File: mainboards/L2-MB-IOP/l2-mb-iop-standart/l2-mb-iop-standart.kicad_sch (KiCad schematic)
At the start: 46 parts, among them J1 URP_Conn_01x12_Socket, J10 GPP_Conn_01x12_Socket, J11 GPP_Conn_01x12_Socket, J12 GPP_Conn_01x12_Socket, J13 GPP_Conn_01x12_Socket, J14 GPP_Conn_01x12_Socket, J15 AIP_Conn_01x12_Socket, J16 AIP_Conn_01x12_Socket, J17 AIP_Conn_01x12_Socket, J18 AIP_Conn_01x12_Socket, J19 ICP_Conn_01x12_Socket, J2 URP_Conn_01x12_Socket, J20 ICP_Conn_01x12_Socket, J21 AIP_Conn_01x12_Socket, J22 AIP_Conn_01x12_Socket, J23 Conn_01x03_Pin, J24 Conn_01x02_Pin, J25 Conn_01x02_Pin, J26 Conn_01x02_Pin, J27 Conn_01x03_Pin, J28 Conn_01x02_Pin, J29 Conn_01x02_Pin, J3 GPP_Conn_01x12_Socket, J4 GPP_Conn_01x12_Socket, J5 GPP_Conn_01x12_Socket, J6 GPP_Conn_01x12_Socket, J7 GPP_Conn_01x12_Socket, J8 GPP_Conn_01x12_Socket, J9 GPP_Conn_01x12_Socket, SW1 SW_SPDT, U1 LM2596s_module, U2 LM2596_mini_module

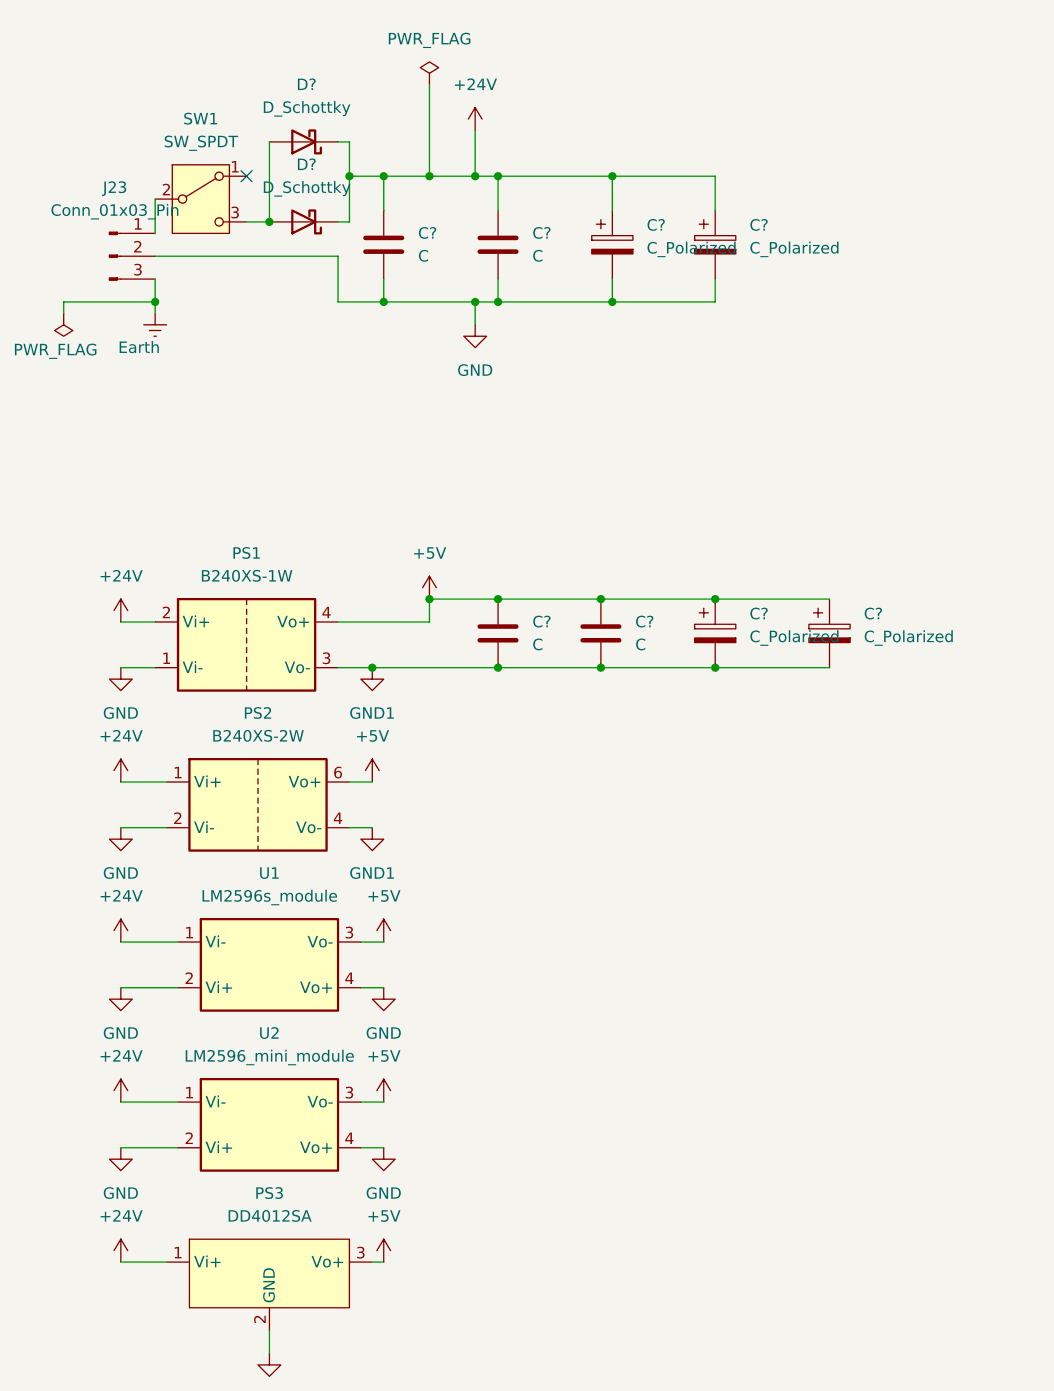
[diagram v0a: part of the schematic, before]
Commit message: Trying to place all jumpers on board.
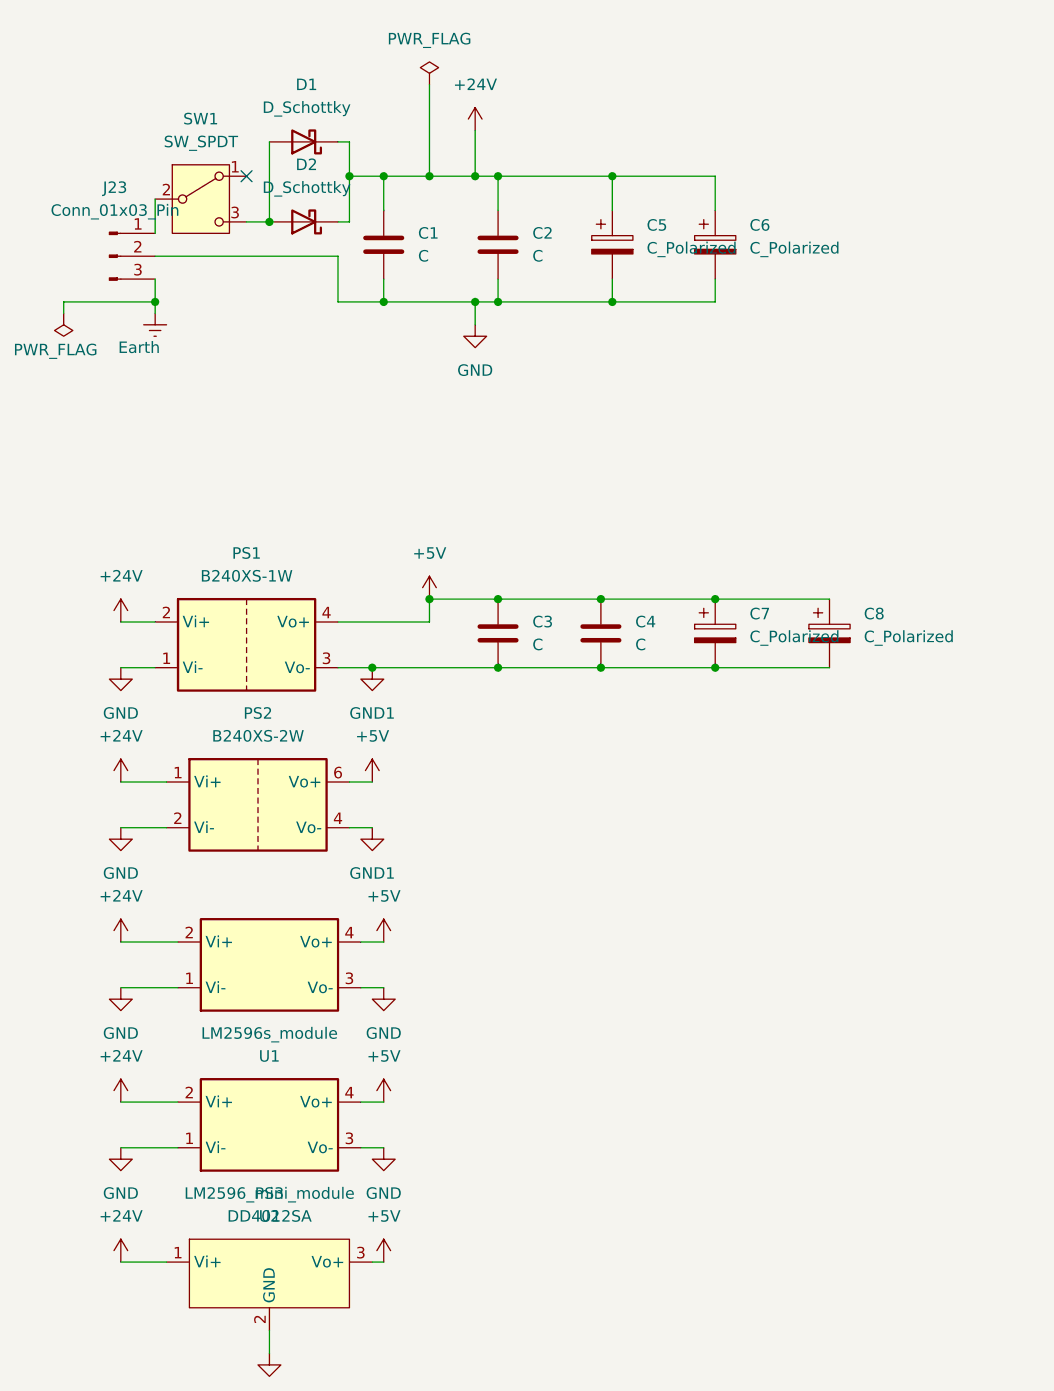
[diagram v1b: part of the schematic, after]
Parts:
- C2, C4: renamed from C?; footprint Capacitor_SMD:C_0402_1005Metric -> Capacitor_SMD:C_0805_2012Metric_Pad1.18x1.45mm_HandSolder
- gave numbers to parts that had none: 8
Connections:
- net +24V: now also U1.2 (Vi+), U2.2 (Vi+); no longer U1.1 (Vi-), U2.1 (Vi-)
- net +5V: now also U1.4 (Vo+), U2.4 (Vo+); no longer U1.3 (Vo-), U2.3 (Vo-)
- net GND: now also U1.1 (Vi-), U1.3 (Vo-), U2.1 (Vi-), U2.3 (Vo-); no longer U1.2 (Vi+), U1.4 (Vo+), U2.2 (Vi+), U2.4 (Vo+)
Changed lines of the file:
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@@
 		(dnp no)
 		(fields_autoplaced yes)
-		(property "Reference" "C?"
+		(property "Reference" "C6"
 			(at 97.79 42.2909 0)
 			(effects
@@
 			(project "l2-mb-iop-standart"
 				(path "/f25cfa12-e490-4a92-ab8c-1b3ce123d4e0"
-					(reference "C?")
+					(reference "C6")
 					(unit 1)
 				)
@@
 		(dnp no)
 		(fields_autoplaced yes)
-		(property "Reference" "C?"
+		(property "Reference" "C5"
 			(at 86.36 42.2909 0)
 			(effects
@@
 			(project ""
 				(path "/f25cfa12-e490-4a92-ab8c-1b3ce123d4e0"
-					(reference "C?")
+					(reference "C5")
 					(unit 1)
 				)
@@
 		(dnp no)
 		(fields_autoplaced yes)
-		(property "Reference" "D?"
+		(property "Reference" "D2"
 			(at 48.5775 35.56 0)
 			(effects
@@
 			(project ""
 				(path "/f25cfa12-e490-4a92-ab8c-1b3ce123d4e0"
-					(reference "D?")
+					(reference "D2")
 					(unit 1)
 				)
@@
 		(lib_id "tuxmio:LM2596_mini_module")
 		(at 44.45 142.24 0)
+		(mirror x)
 		(unit 1)
 		(exclude_from_sim no)
@@
 		(on_board yes)
 		(dnp no)
-		(fields_autoplaced yes)
 		(property "Reference" "U2"
-			(at 44.45 132.08 0)
+			(at 44.45 152.4 0)
 			(effects
 				(font
@@
 		)
 		(property "Value" "LM2596_mini_module"
-			(at 44.45 134.62 0)
+			(at 44.45 149.86 0)
 			(effects
 				(font
@@
 		)
 		(property "Footprint" "tuxmio:LM2596_mini_module"
-			(at 44.958 150.114 0)
+			(at 44.958 134.366 0)
 			(effects
 				(font
@@
 		)
 		(property "Description" "3W, non isolated DC/DC converter"
-			(at 44.45 151.892 0)
+			(at 44.45 132.588 0)
 			(effects
 				(font
@@
 		(dnp no)
 		(fields_autoplaced yes)
-		(property "Reference" "C?"
+		(property "Reference" "C1"
 			(at 60.96 43.1799 0)
 			(effects
@@
 			(project ""
 				(path "/f25cfa12-e490-4a92-ab8c-1b3ce123d4e0"
-					(reference "C?")
+					(reference "C1")
 					(unit 1)
 				)
@@
 		(dnp no)
 		(fields_autoplaced yes)
-		(property "Reference" "C?"
+		(property "Reference" "C7"
 			(at 97.79 85.4709 0)
 			(effects
@@
 			(project ""
 				(path "/f25cfa12-e490-4a92-ab8c-1b3ce123d4e0"
-					(reference "C?")
+					(reference "C7")
 					(unit 1)
 				)
@@
 		(dnp no)
 		(fields_autoplaced yes)
-		(property "Reference" "D?"
+		(property "Reference" "D1"
 			(at 48.5775 26.67 0)
 			(effects
@@
 			(project "l2-mb-iop-standart"
 				(path "/f25cfa12-e490-4a92-ab8c-1b3ce123d4e0"
-					(reference "D?")
+					(reference "D1")
 					(unit 1)
 				)
@@
 		(dnp no)
 		(fields_autoplaced yes)
-		(property "Reference" "C?"
+		(property "Reference" "C8"
 			(at 110.49 85.4709 0)
 			(effects
@@
 			(project "l2-mb-iop-standart"
 				(path "/f25cfa12-e490-4a92-ab8c-1b3ce123d4e0"
-					(reference "C?")
+					(reference "C8")
 					(unit 1)
 				)
@@
 		(dnp no)
 		(fields_autoplaced yes)
-		(property "Reference" "C?"
+		(property "Reference" "C4"
 			(at 85.09 86.3599 0)
 			(effects
@@
 			)
 		)
-		(property "Footprint" "Capacitor_SMD:C_0402_1005Metric"
+		(property "Footprint" "Capacitor_SMD:C_0805_2012Metric_Pad1.18x1.45mm_HandSolder"
 			(at 82.2452 91.44 0)
 			(effects
@@
 			(project "l2-mb-iop-standart"
 				(path "/f25cfa12-e490-4a92-ab8c-1b3ce123d4e0"
-					(reference "C?")
+					(reference "C4")
 					(unit 1)
 				)
@@
 		(dnp no)
 		(fields_autoplaced yes)
-		(property "Reference" "C?"
+		(property "Reference" "C2"
 			(at 73.66 43.1799 0)
 			(effects
@@
 			)
 		)
-		(property "Footprint" "Capacitor_SMD:C_0402_1005Metric"
+		(property "Footprint" "Capacitor_SMD:C_0805_2012Metric_Pad1.18x1.45mm_HandSolder"
 			(at 70.8152 48.26 0)
 			(effects
@@
 			(project "l2-mb-iop-standart"
 				(path "/f25cfa12-e490-4a92-ab8c-1b3ce123d4e0"
-					(reference "C?")
+					(reference "C2")
 					(unit 1)
 				)
@@
 		(lib_id "tuxmio:LM2596s_module")
 		(at 44.45 124.46 0)
+		(mirror x)
 		(unit 1)
 		(exclude_from_sim no)
@@
 		(on_board yes)
 		(dnp no)
-		(fields_autoplaced yes)
 		(property "Reference" "U1"
-			(at 44.45 114.3 0)
+			(at 44.45 134.62 0)
 			(effects
 				(font
@@
 		)
 		(property "Value" "LM2596s_module"
-			(at 44.45 116.84 0)
+			(at 44.45 132.08 0)
 			(effects
 				(font
@@
 		)
 		(property "Footprint" "tuxmio:LM2596s_module"
-			(at 44.704 132.588 0)
+			(at 44.704 116.332 0)
 			(effects
 				(font
@@
 		)
 		(property "Description" "3W, non isolated DC/DC converter"
-			(at 45.212 134.366 0)
+			(at 45.212 114.554 0)
 			(effects
 				(font
@@
 		(dnp no)
 		(fields_autoplaced yes)
-		(property "Reference" "C?"
+		(property "Reference" "C3"
 			(at 73.66 86.3599 0)
 			(effects
@@
 			(project ""
 				(path "/f25cfa12-e490-4a92-ab8c-1b3ce123d4e0"
-					(reference "C?")
+					(reference "C3")
 					(unit 1)
 				)

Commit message: Trying to place everithing on board
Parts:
- removed J27: Conn_01x03_Pin, Connector_PinHeader_2.54mm:PinHeader_1x03_P2.54mm_Vertical, symbol Connector:Conn_01x03_Pin
- added J27: Conn_01x02_Pin, Connector_PinHeader_2.54mm:PinHeader_1x02_P2.54mm_Vertical, symbol Connector:Conn_01x02_Pin
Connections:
- net +5V: now also J27.1 (Pin_1)
- net GND1: no longer A1.4 (GND)
- net at A1.18 (AREF), J15.2 (A_Ref), J16.2 (A_Ref)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: now also J27.2 (Pin_2)
- net at A1.28 (~{RESET}), J28.1 (Pin_1): no longer A1.3 (~{RESET})
- no-connect marks 60 -> 61
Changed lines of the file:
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@@
 	)
 	(junction
-		(at 303.53 147.32)
-		(diameter 0)
-		(color 0 0 0 0)
-	)
-	(junction
 		(at 303.53 210.82)
 		(diameter 0)
@@
 	)
 	(junction
-		(at 265.43 134.62)
-		(diameter 0)
-		(color 0 0 0 0)
-	)
-	(junction
 		(at 321.31 210.82)
 		(diameter 0)
@@
 	)
 	(no_connect
-		(at 266.7 190.5)
+		(at 303.53 147.32)
 	)
 	(no_connect
-		(at 275.59 185.42)
+		(at 266.7 190.5)
 	)
 	(no_connect
-		(at 237.49 123.19)
+		(at 275.59 185.42)
 	)
 	(no_connect
@@
 	)
 	(no_connect
+		(at 265.43 134.62)
+	)
+	(no_connect
 		(at 280.67 86.36)
 	)
@@
 	(wire
 		(pts
+			(xy 303.53 144.78) (xy 307.34 144.78)
+		)
+		(stroke
+			(width 0)
+			(type default)
+		)
+	)
+	(wire
+		(pts
 			(xy 196.85 67.31) (xy 204.47 67.31)
 		)
@@
 	(wire
 		(pts
-			(xy 237.49 130.81) (xy 265.43 130.81)
+			(xy 237.49 130.81) (xy 262.89 130.81)
 		)
 		(stroke
@@
 	(wire
 		(pts
-			(xy 303.53 144.78) (xy 303.53 147.32)
-		)
-		(stroke
-			(width 0)
-			(type default)
-		)
-	)
-	(wire
-		(pts
 			(xy 303.53 208.28) (xy 312.42 208.28)
 		)
@@
 	(wire
 		(pts
-			(xy 303.53 147.32) (xy 307.34 147.32)
-		)
-		(stroke
-			(width 0)
-			(type default)
-		)
-	)
-	(wire
-		(pts
 			(xy 273.05 120.65) (xy 251.46 120.65)
 		)
@@
 	(wire
 		(pts
+			(xy 307.34 148.59) (xy 307.34 144.78)
+		)
+		(stroke
+			(width 0)
+			(type default)
+		)
+	)
+	(wire
+		(pts
 			(xy 284.48 210.82) (xy 293.37 210.82)
 		)
@@
 	(wire
 		(pts
-			(xy 265.43 134.62) (xy 265.43 130.81)
-		)
-		(stroke
-			(width 0)
-			(type default)
-		)
-	)
-	(wire
-		(pts
 			(xy 196.85 78.74) (xy 254 78.74)
 		)
@@
 	(wire
 		(pts
-			(xy 262.89 134.62) (xy 265.43 134.62)
+			(xy 262.89 130.81) (xy 262.89 134.62)
 		)
 		(stroke
@@
 	(symbol
 		(lib_id "power:GND1")
-		(at 307.34 147.32 0)
+		(at 307.34 148.59 0)
 		(unit 1)
 		(exclude_from_sim no)
@@
 		(fields_autoplaced yes)
 		(property "Reference" "#PWR25"
-			(at 307.34 153.67 0)
+			(at 307.34 154.94 0)
 			(effects
 				(font
@@
 		)
 		(property "Value" "GND1"
-			(at 307.34 152.4 0)
+			(at 307.34 153.67 0)
 			(effects
 				(font
@@
 		)
 		(property "Footprint" ""
-			(at 307.34 147.32 0)
+			(at 307.34 148.59 0)
 			(effects
 				(font
@@
 		)
 		(property "Datasheet" ""
-			(at 307.34 147.32 0)
+			(at 307.34 148.59 0)
 			(effects
 				(font
@@
 		)
 		(property "Description" "Power symbol creates a global label with name \"GND1\" , ground"
-			(at 307.34 147.32 0)
+			(at 307.34 148.59 0)
 			(effects
 				(font
@@
 			)
 		)
-		(property "Description" "Generic connector, single row, 01x02, script generated"
-			(at 232.41 130.81 0)
+		(property "Description" "Connector for reset external button."
+			(at 213.614 125.222 0)
 			(effects
 				(font
 					(size 1.27 1.27)
 				)
-				(hide yes)
 			)
 		)
@@
 	)
 	(symbol
-		(lib_id "Connector:Conn_01x03_Pin")
-		(at 232.41 120.65 0)
-		(unit 1)
-		(exclude_from_sim no)
-		(in_bom yes)
-		(on_board yes)
-		(dnp no)
-		(fields_autoplaced yes)
-		(property "Reference" "J27"
-			(at 233.045 113.03 0)
-			(effects
-				(font
-					(size 1.27 1.27)
-				)
-			)
-		)
-		(property "Value" "Conn_01x03_Pin"
-			(at 233.045 115.57 0)
-			(effects
-				(font
-					(size 1.27 1.27)
-				)
-			)
-		)
-		(property "Footprint" "Connector_PinHeader_2.54mm:PinHeader_1x03_P2.54mm_Vertical"
-			(at 232.41 120.65 0)
-			(effects
-				(font
-					(size 1.27 1.27)
-				)
-				(hide yes)
-			)
-		)
-		(property "Datasheet" "~"
-			(at 232.41 120.65 0)
-			(effects
-				(font
-					(size 1.27 1.27)
-				)
-				(hide yes)
-			)
-		)
-		(property "Description" "Generic connector, single row, 01x03, script generated"
-			(at 232.41 120.65 0)
-			(effects
-				(font
-					(size 1.27 1.27)
-				)
-				(hide yes)
-			)
-		)
-		(pin "3"
-		)
-		(pin "1"
-		)
-		(pin "2"
-		)
-		(instances
-			(project ""
-				(path "/f25cfa12-e490-4a92-ab8c-1b3ce123d4e0"
-					(reference "J27")
-					(unit 1)
-				)
-			)
-		)
-	)
-	(symbol
 		(lib_id "tuxmio:B240XS-1W")
 		(at 41.91 88.9 0)
@@
 			)
 		)
-		(property "Description" "Generic connector, single row, 01x02, script generated"
-			(at 232.41 153.67 0)
+		(property "Description" "Jumper for VIN"
+			(at 223.774 148.59 0)
 			(effects
 				(font
 					(size 1.27 1.27)
 				)
-				(hide yes)
 			)
 		)
@@
 	)
 	(symbol
+		(lib_id "Connector:Conn_01x02_Pin")
+		(at 232.41 118.11 0)
+		(unit 1)
+		(exclude_from_sim no)
+		(in_bom yes)
+		(on_board yes)
+		(dnp no)
+		(property "Reference" "J27"
+			(at 233.045 113.03 0)
+			(effects
+				(font
+					(size 1.27 1.27)
+				)
+			)
+		)
+		(property "Value" "Conn_01x02_Pin"
+			(at 230.886 115.316 0)
+			(effects
+				(font
+					(size 1.27 1.27)
+				)
+			)
+		)
+		(property "Footprint" "Connector_PinHeader_2.54mm:PinHeader_1x02_P2.54mm_Vertical"
+			(at 232.41 118.11 0)
+			(effects
+				(font
+					(size 1.27 1.27)
+				)
+				(hide yes)
+			)
+		)
+		(property "Datasheet" "~"
+			(at 232.41 118.11 0)
+			(effects
+				(font
+					(size 1.27 1.27)
+				)
+				(hide yes)
+			)
+		)
+		(property "Description" "Connector for AREF.  Jumper for +5VDC"
+			(at 211.074 113.03 0)
+			(effects
+				(font
+					(size 1.27 1.27)
+				)
+			)
+		)
+		(pin "2"
+		)
+		(pin "1"
+		)
+		(instances
+			(project "l2-mb-iop-standart"
+				(path "/f25cfa12-e490-4a92-ab8c-1b3ce123d4e0"
+					(reference "J27")
+					(unit 1)
+				)
+			)
+		)
+	)
+	(symbol
 		(lib_id "power:+5V")
 		(at 55.88 104.14 0)
@@
 			)
 		)
-		(property "Description" "Generic connector, single row, 01x02, script generated"
-			(at 232.41 142.24 0)
+		(property "Description" "Jumper for 5V/3V3"
+			(at 220.98 137.414 0)
 			(effects
 				(font
 					(size 1.27 1.27)
 				)
-				(hide yes)
 			)
 		)
@@
 			)
 		)
-		(property "Description" "Generic connector, single row, 01x02, script generated"
-			(at 191.77 76.2 0)
+		(property "Description" "Connecting GND and bipolar PS midpoint if it is not required galvanic seperation"
+			(at 150.622 71.12 0)
 			(effects
 				(font
 					(size 1.27 1.27)
 				)
-				(hide yes)
 			)
 		)
@@
 			)
 		)
-		(property "Description" "Generic connector, single row, 01x02, script generated"
-			(at 191.77 64.77 0)
+		(property "Description" "Connecting GND and GND1 if it is not required galvanic seperation"
+			(at 157.988 59.436 0)
 			(effects
 				(font
 					(size 1.27 1.27)
 				)
-				(hide yes)
 			)
 		)

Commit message: Board first version
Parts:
- removed C1, C3: C, Capacitor_THT:C_Disc_D4.3mm_W1.9mm_P5.00mm, symbol Device:C
- removed C5, C7: C_Polarized, Capacitor_THT:CP_Radial_D6.3mm_P2.50mm, symbol Device:C_Polarized
- removed D2: D_Schottky, Diode_THT:D_DO-15_P10.16mm_Horizontal, symbol Device:D_Schottky
- removed J24, J25, J26, J27, J28, J29: Conn_01x02_Pin, Connector_PinHeader_2.54mm:PinHeader_1x02_P2.54mm_Vertical, symbol Connector:Conn_01x02_Pin
- removed PS2: B240XS-2W, tuxmio:B240XS-2W, symbol tuxmio:B240XS-2W
- removed SW1: SW_SPDT, tuxmio:SW-SPDT_1x03_P2.54mm_Vertical, symbol Switch:SW_SPDT
- removed U1: LM2596s_module, tuxmio:LM2596s_module, symbol tuxmio:LM2596s_module
- removed U2: LM2596_mini_module, tuxmio:LM2596_mini_module, symbol tuxmio:LM2596_mini_module
- added J10, J11, J12, J13, J2, J3, J4, J5, J6, J7, J8, J9: Conn_01x01_Pin, Connector_PinHeader_1.00mm:PinHeader_1x01_P1.00mm_Vertical, symbol Connector:Conn_01x01_Pin
- J1: renamed from J23; footprint Connector_Phoenix_MC_HighVoltage:PhoenixContact_MCV_1,5_3-G-5.08_1x03_P5.08mm_Vertical -> Connector_PinHeader_2.54mm:PinHeader_1x03_P2.54mm_Vertical
- renumbered C2 to C1, C6 to C2, C4 to C3, C8 to C4, J1 to J14, J2 to J15, J3 to J16, J4 to J17, J5 to J18, J6 to J19, J7 to J20, J8 to J21, J9 to J22, J10 to J23, J11 to J24, J12 to J25, J13 to J26, J14 to J27, J15 to J28, J16 to J29, J17 to J30, J18 to J31, J19 to J32, J20 to J33, J21 to J34, J22 to J35, PS3 to PS2
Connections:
- net +5V: now also J10.1 (Pin_1), J12.1 (Pin_1), J6.1 (Pin_1)
- net 0V_bipolar: now also J5.1 (Pin_1)
- net GND: now also J3.1 (Pin_1), J4.1 (Pin_1)
- net GND1: now also J2.1 (Pin_1), J9.1 (Pin_1)
- net at A1.18 (AREF), J28.2 (A_Ref), J29.2 (A_Ref)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: now also J7.1 (Pin_1)
- net at J1.1 (Pin_1): now also D1.2 (A)
- net at A1.28 (~{RESET}): now also J8.1 (Pin_1)
- net at A1.30 (VIN): now also J13.1 (Pin_1)
- net at A1.17 (3V3): now also J11.1 (Pin_1)
- no-connect marks 61 -> 60
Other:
- note added: "note for future Mega 2560 has 54 digital input/output pins, of which 14 can be used for PWM output. + It also has 16 analog input pins in addition. End part 2x18-2x5V-2xGND"
- note removed: "note for future Mega 2560 has 54 digital input/output pins, of which 14 can be used for PWM output. + It also has 16 analog input pins in addition."
- moved on the sheet: C3, C4, PS2

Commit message: Started first DO board
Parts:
- C1, C3: footprint Capacitor_SMD:C_0805_2012Metric_Pad1.18x1.45mm_HandSolder -> (none)
- C2, C4: footprint Capacitor_SMD:CP_Elec_4x5.3 -> (none)
- D1: footprint Diode_SMD:D_1206_3216Metric -> (none)
- J1: footprint Connector_PinHeader_2.54mm:PinHeader_1x03_P2.54mm_Vertical -> (none)
- J10, J11, J12, J13, J2, J3, J4, J5, J6, J7, J8, J9: footprint Connector_PinHeader_1.00mm:PinHeader_1x01_P1.00mm_Vertical -> (none)
- J14, J15: footprint tuxmio:MB_URP_socket_PinHeader_1x12_P2.54mm_Vertical -> tuxmio:MB_URP_PinSocket_1x12_P2.54mm_Vertical
- J16, J17, J18, J19, J20, J21, J22, J23, J24, J25, J26, J27: footprint tuxmio:MB_GPP_socket_PinHeader_1x12_P2.54mm_Vertical -> tuxmio:MB_GPP_PinSocket_1x12_P2.54mm_Vertical
- J28, J29, J30, J31, J34, J35: footprint tuxmio:MB_AIP_socket_PinHeader_1x12_P2.54mm_Vertical -> tuxmio:MB_AIP_PinSocket_1x12_P2.54mm_Vertical
- J32, J33: footprint tuxmio:MB_ICP_socket_PinHeader_1x12_P2.54mm_Vertical -> tuxmio:MB_ICP_PinSocket_1x12_P2.54mm_Vertical
